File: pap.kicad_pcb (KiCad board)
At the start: 2 copper layers, 60 x 60 mm, 44 parts, among them J1 Conn_01x02, J3 Conn_01x04, J6 Conn_01x02, U1 powerstep01

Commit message: sigo ruteando y acomodando ocsas, agrego algunos leds
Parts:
- added D203: LED, pap:led5p_rj, F.Cu at (101.5, 111.2)
- added D204: LED, pap:led5p_rj, F.Cu at (101.5, 130.5)
- added R203: R, Resistor_SMD:R_0805_2012Metric, F.Cu at (105.1, 111.2)
- added R204: R, Resistor_SMD:R_0805_2012Metric, F.Cu at (104.8, 130.5)
- C4, C5: footprint Capacitor_SMD:C_0805_2012Metric -> Capacitor_SMD:C_1206_3216Metric_Pad1.42x1.75mm_HandSolder
- D10, D202, D8: value LED -> LED_I; footprint LED_SMD:LED_0805_2012Metric -> pap:led5p_enchufable
- D11, D7: footprint LED_SMD:LED_0805_2012Metric -> pap:led5p_enchufable
- D4, D5, D6: footprint LED_SMD:LED_0805_2012Metric -> pap:led5p_rj
- R11, R12, R13, R14, R202: moved to B.Cu
- moved D10 78.5 mm to (144.6, 89.8)
- moved D4 78.1 mm to (101.5, 92.0), turned to 270 degrees
- moved R13 74.3 mm to (140.0, 89.5), turned to 0 degrees
- moved R8 73.3 mm to (104.8, 92.0), turned to 180 degrees
- moved D11 72.0 mm to (144.8, 97.0)
- moved R14 71.1 mm to (139.9, 93.0), turned to 0 degrees
- moved D6 66.9 mm to (101.5, 102.0), turned to 270 degrees
- moved D202 64.3 mm to (144.5, 113.5), turned to 90 degrees
- moved R10 62.3 mm to (104.8, 102.0), turned to 180 degrees
- moved R202 57.5 mm to (144.5, 107.5), turned to 270 degrees
- moved D5 49.9 mm to (101.5, 120.5), turned to 270 degrees
- moved R9 44.9 mm to (105.0, 120.5), turned to 180 degrees
- moved D8 40.8 mm to (144.5, 130.5)
- moved D7 36.1 mm to (144.5, 137.6)
- moved C7 3.35 mm to (140.5, 122.0)
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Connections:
- D10 pad 1: Net-(D10-Pad1) -> /connector/MotorA2
- D10 pad 2: /connector/MotorB1 -> Net-(D10-Pad2)
- D11 pad 2: /connector/MotorB2 -> /connector/MotorA1
- D202 pad 1: Net-(D202-Pad1) -> 85v
- D202 pad 2: 85v -> Net-(D202-Pad2)
- D7 pad 2: /connector/MotorA1 -> /connector/MotorB2
- D8 pad 1: Net-(D8-Pad1) -> /connector/MotorB1
- D8 pad 2: /connector/MotorA2 -> Net-(D8-Pad2)
- R12 pad 2: Net-(D8-Pad1) -> Net-(D8-Pad2)
- R13 pad 2: Net-(D10-Pad1) -> Net-(D10-Pad2)
- R202 pad 2: Net-(D202-Pad1) -> Net-(D202-Pad2)
- U1 pad 16: /motor/flag -> /motor/Flag
- rJ303 pad 1: G3V3 -> 3v3
- rJ303 pad 3: /connector/Switch -> Net-(rJ303-Pad3)
- rJ303 pad 5: Net-(rJ303-Pad5) -> /connector/Switch
- rJ303 pad 6: 3v3 -> G3V3
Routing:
- net 85v: track 202.7 -> 182.6 mm
- net /connector/Osc_Out: track 24.6 -> 20.1 mm
- net /connector/MotorA2: track 52.2 -> 56.2 mm
- net /connector/MotorA1: track 41.2 -> 44.7 mm
- net Net-(D202-Pad2): track 0.00 -> 2.52 mm
- net 3v3: track 26.0 -> 23.7 mm
- net /motor/Adc: track 46.1 -> 43.9 mm
- net Net-(C5-Pad2): track 7.76 -> 5.61 mm
- net /motor/Cpump: track 7.58 -> 9.36 mm
- net /connector/Osc_In: track 23.2 -> 21.9 mm
- net /motor/Vboot: track 13.7 -> 14.7 mm
- net G85V: track 99.4 -> 99.3 mm, vias 20 -> 19
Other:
- net class HV: clearance 1 -> 0.5
- net class Mid_Power: clearance 0.4 -> 0.3
- net class Power: clearance 0.6 -> 0.4

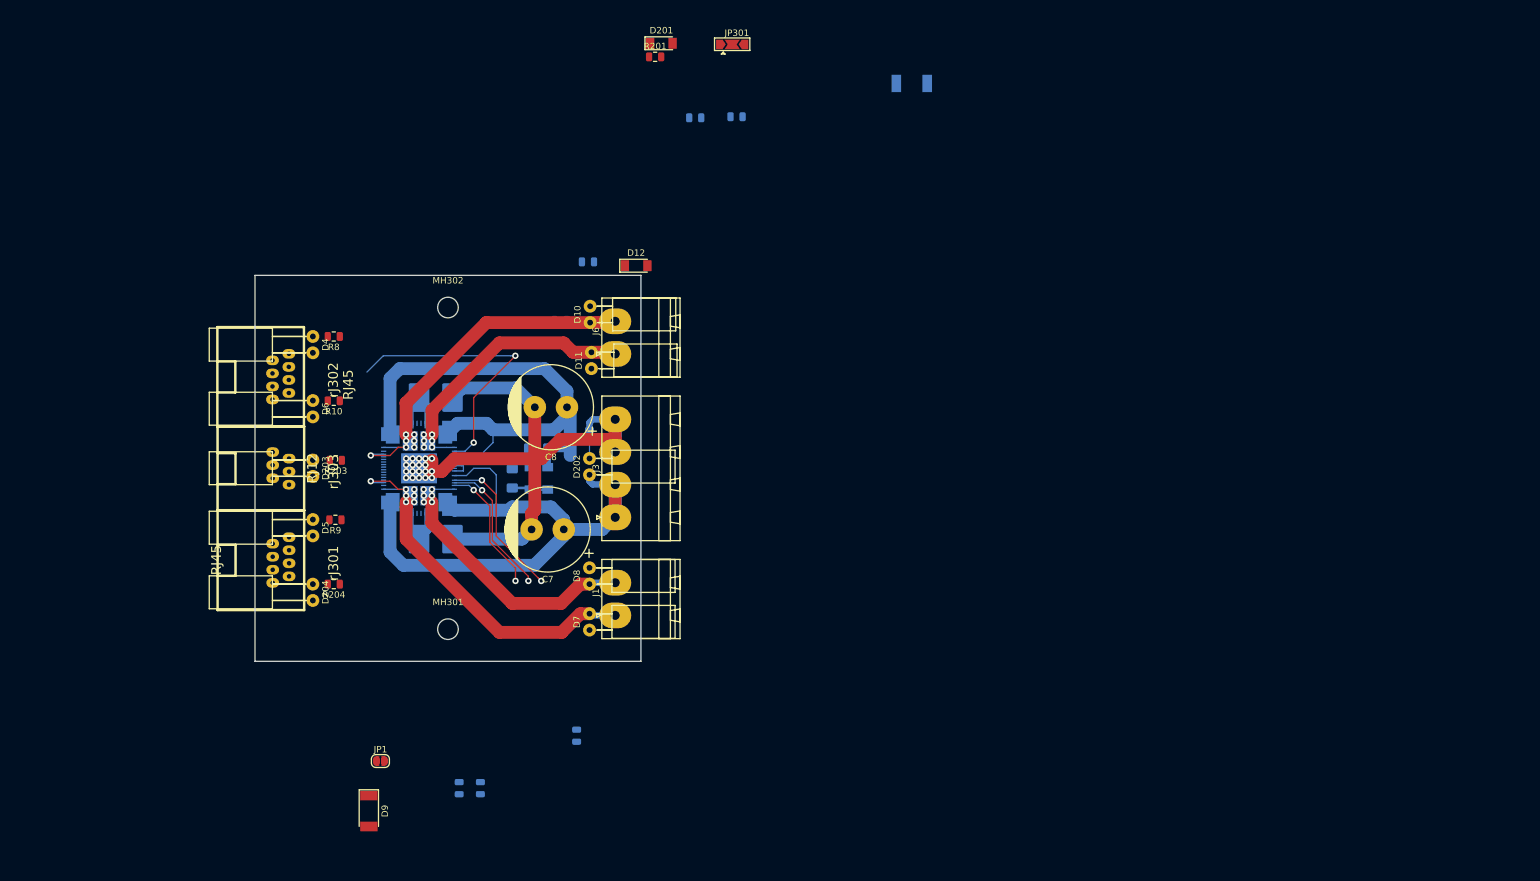
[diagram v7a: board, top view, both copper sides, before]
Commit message: ruteo!! no se como pero esta todo conectado!, horrible claro
conecto todo.. bastamte ofiero pero conecto.. y quedan huevos para ir
mejorando.. tampoco esta taaaan mal... y las cosas ya estan en su
lugar.. me quedan varias horas para pulir todo y respetar las reglas de
cada net y demas.. queda un pedazo todavia pero no esta nada mal..
lo que si me di cuenta que estaba pensando mal lo de la cadena de spi y
la de osci, ahora es simple, ficha de in y ficha de out, por la de in
entra sdi y por la de out sale sdo. el ultimo cierra la puerta puentendo
su sdo con un pin suelto de sdo_back que lleva hacia atras el sdo final
y lo termina mandando al uC. o sea es un pin dedicado todo puenteado que
termina en el pin del uC. y para el osci es mas facil porque no necesita
retorno, es una cadena solo de ida, con la salvedad de que por sof,
configuro el primero de la cadena para que genere el osc por sdo y el
segundo mete sdo por el pin de sdi y lo configuro como inversor y asi
siguiendo. no necesita selector de nada, es todo por sof. y despues fui
acomodando un poco el pinout y no mucho mas.. el camino del osci es
larguirucho y lleno de vias pero ese si que quedo atascado y no supe
como sacarlo sin dar una supervuelta.. esperemos que resista..
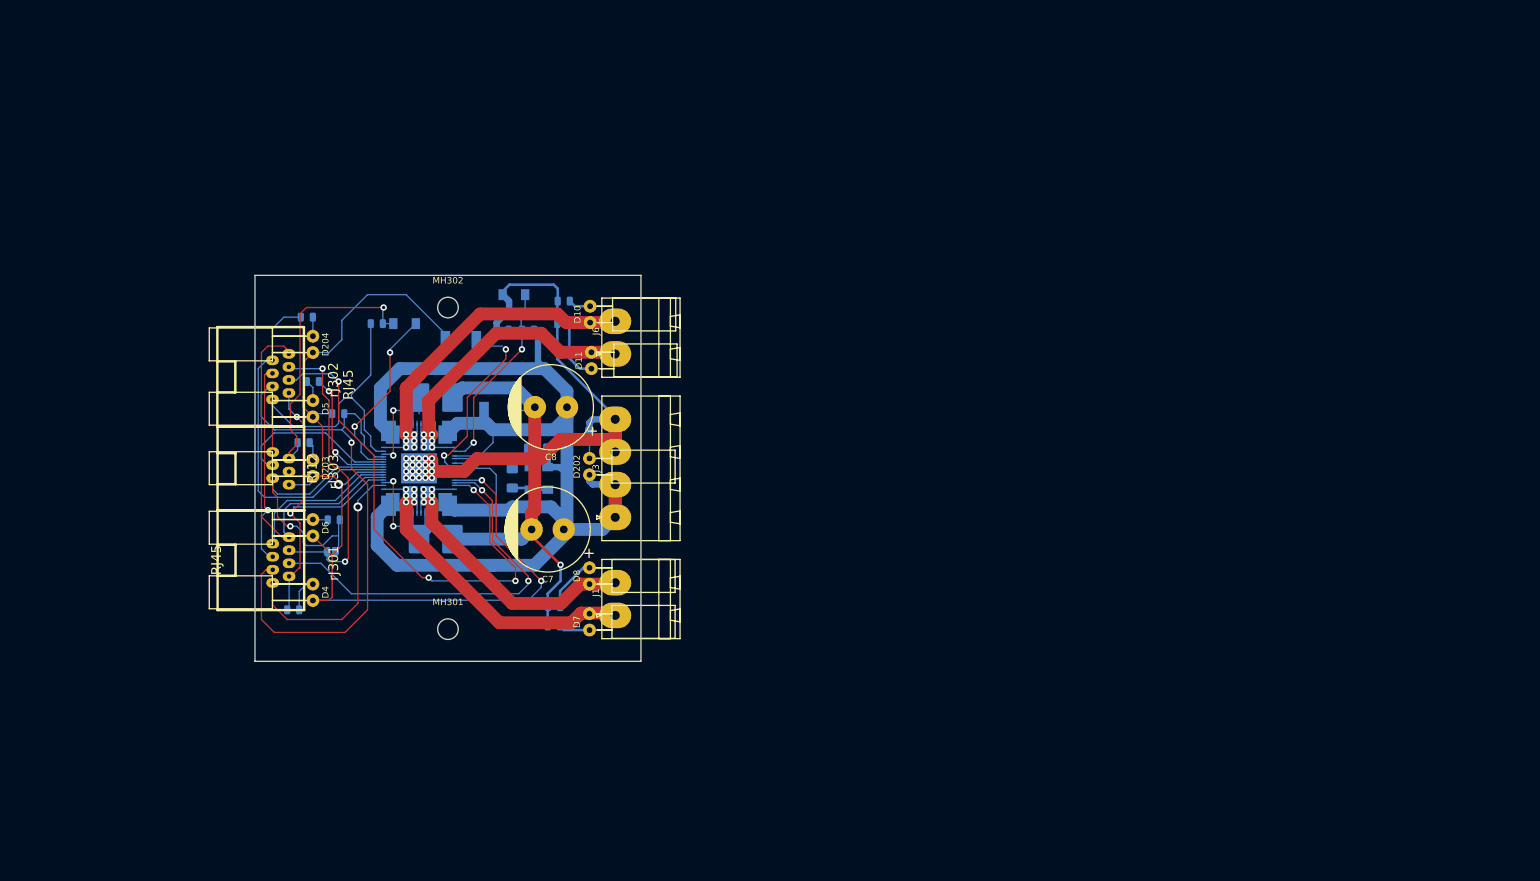
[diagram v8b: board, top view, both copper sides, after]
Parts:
- removed JP301: Clk_Select, Jumper:SolderJumper-3_P2.0mm_Open_TrianglePad1.0x1.5mm
- D12, D201, D9, JP1, R10, R201, R203, R204, R8, R9: moved to B.Cu
- moved D1 81.8 mm to (130.5, 103.5)
- moved D9 74.7 mm to (124.5, 92.5), turned to 180 degrees
- moved R201 74.2 mm to (105.4, 104.0), turned to 180 degrees
- moved C6 66.3 mm to (132.9, 88.5), turned to 0 degrees
- moved D201 59.1 mm to (115.8, 90.0)
- moved C1 58.9 mm to (111.4, 90.0)
- moved R6 46.4 mm to (134.9, 91.0), turned to 180 degrees
- moved R8 43.0 mm to (98.4, 134.5), turned to 0 degrees
- moved R204 41.7 mm to (100.6, 89.0), turned to 0 degrees
- moved D204 38.5 mm to (101.5, 92.0)
- moved D4 38.5 mm to (101.5, 130.5)
- moved JP1 33.4 mm to (104.3, 125.5)
- moved R12 30.5 mm to (139.0, 134.0), turned to 0 degrees
- moved R11 29.2 mm to (138.9, 137.0), turned to 0 degrees
- moved R9 21.8 mm to (101.5, 99.0)
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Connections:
- net /connector/Sdo_Chain renamed /connector/Sdo_Back
- rJ301 pad 2: /connector/Busy_Out -> /connector/CS
- rJ301 pad 4: /connector/Osc -> /connector/Osc_In
- rJ301 pad 6: /connector/SDI -> /connector/Busy_Out
- rJ301 pad 7: /connector/CLK -> /connector/SDI
- rJ301 pad 8: /connector/CS -> /connector/CLK
- rJ302 pad 2: /connector/Busy_Out -> /connector/CS
- rJ302 pad 4: /connector/Osc -> /connector/Osc_Out
- rJ302 pad 6: /connector/SDO -> /connector/Busy_Out
- rJ302 pad 7: /connector/CLK -> /connector/SDO
- rJ302 pad 8: /connector/CS -> /connector/CLK
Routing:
- net 3v3: track 23.7 -> 159.6 mm, vias 2 -> 3
- net /connector/Reset: track 0.00 -> 90.3 mm, vias 0 -> 1
- net G3V3: track 0.00 -> 89.9 mm, vias 0 -> 1
- net G85V: track 99.3 -> 161.2 mm, vias 19 -> 21
- net /connector/Osc_Out: track 20.1 -> 79.3 mm, vias 2 -> 4
- net /connector/CLK: track 0.00 -> 58.7 mm
- net /connector/CS: track 0.00 -> 54.6 mm, vias 0 -> 2
- net /connector/SDO: track 0.00 -> 53.5 mm
- net /connector/Busy_Out: track 0.00 -> 47.6 mm, vias 0 -> 2
- net /connector/Busy: track 0.00 -> 45.4 mm, vias 0 -> 1
- net /connector/Switch: track 0.00 -> 44.6 mm, vias 0 -> 1
- net /connector/Osc_In: track 21.9 -> 62.1 mm
- net /connector/Sdo_Back: track 0.00 -> 31.2 mm, vias 0 -> 1
- net /motor/Switch_Local: track 0.00 -> 28.3 mm, vias 0 -> 2
- net 15v: track 3.60 -> 31.6 mm, vias 0 -> 2
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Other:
- net class Power: via_dia 1.6 -> 1.4; via_drill 1 -> 0.8
